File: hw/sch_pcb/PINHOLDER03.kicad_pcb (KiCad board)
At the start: 2 copper layers, 50.3 x 30 mm, 8 parts, among them J1 HEADER_1x03, M1 HOLE, M2 HOLE, M3 HOLE, M4 HOLE

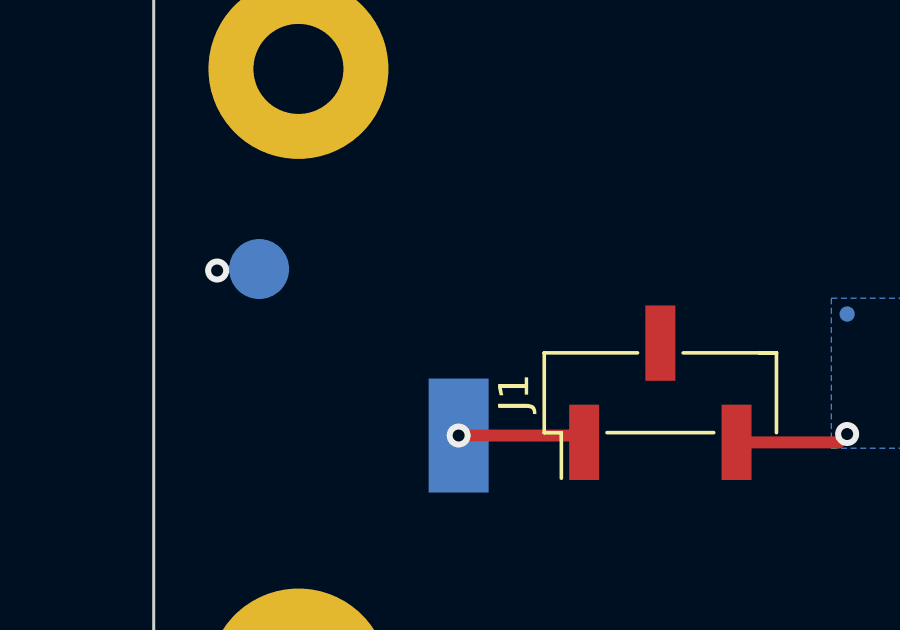
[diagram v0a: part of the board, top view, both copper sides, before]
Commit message: uprava layoutu, 2 diody
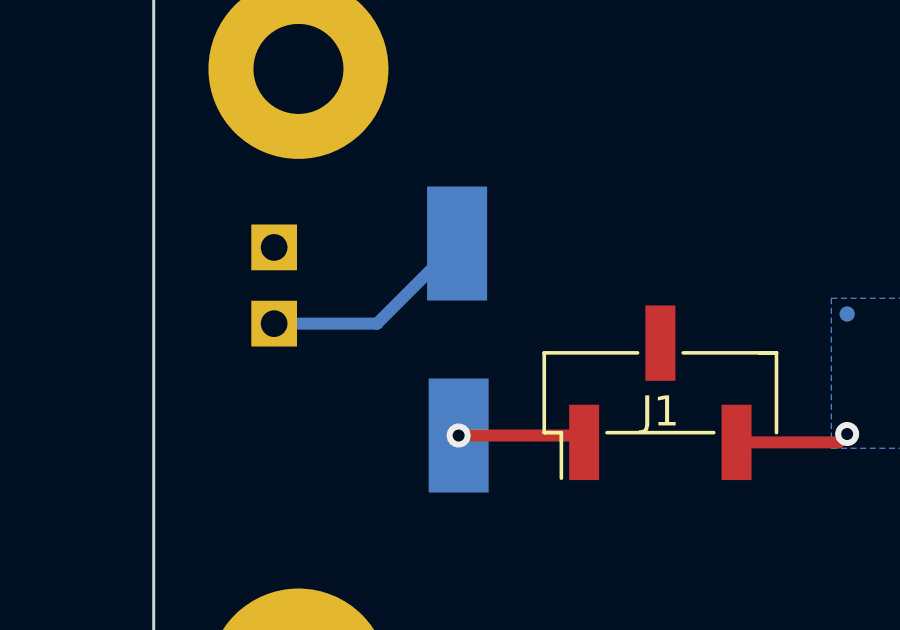
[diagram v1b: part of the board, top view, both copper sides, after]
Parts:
- removed TP3: TestPoint, TestPoint:TestPoint_Pad_D2.0mm
- added J2: HEADER_1x02, Mlab_Pin_Headers:Straight_1x02, B.Cu at (148.8, 83.7)
- added TP4: TestPoint, TestPoint:TestPoint_Keystone_5019_Minature, B.Cu at (154.9, 82.3)
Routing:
- net Net-(D1-Pad2): track 0.00 -> 7.21 mm
- net GND: track 1.42 -> 0.00 mm, vias 1 -> 0
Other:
- board text added: "Mid"
- board text added: "Mid GND"
- board text added: "Top"
- board text removed: "GND"
